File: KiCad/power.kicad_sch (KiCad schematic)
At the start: 13 parts, among them J4 10-pin power header, U1 TL074

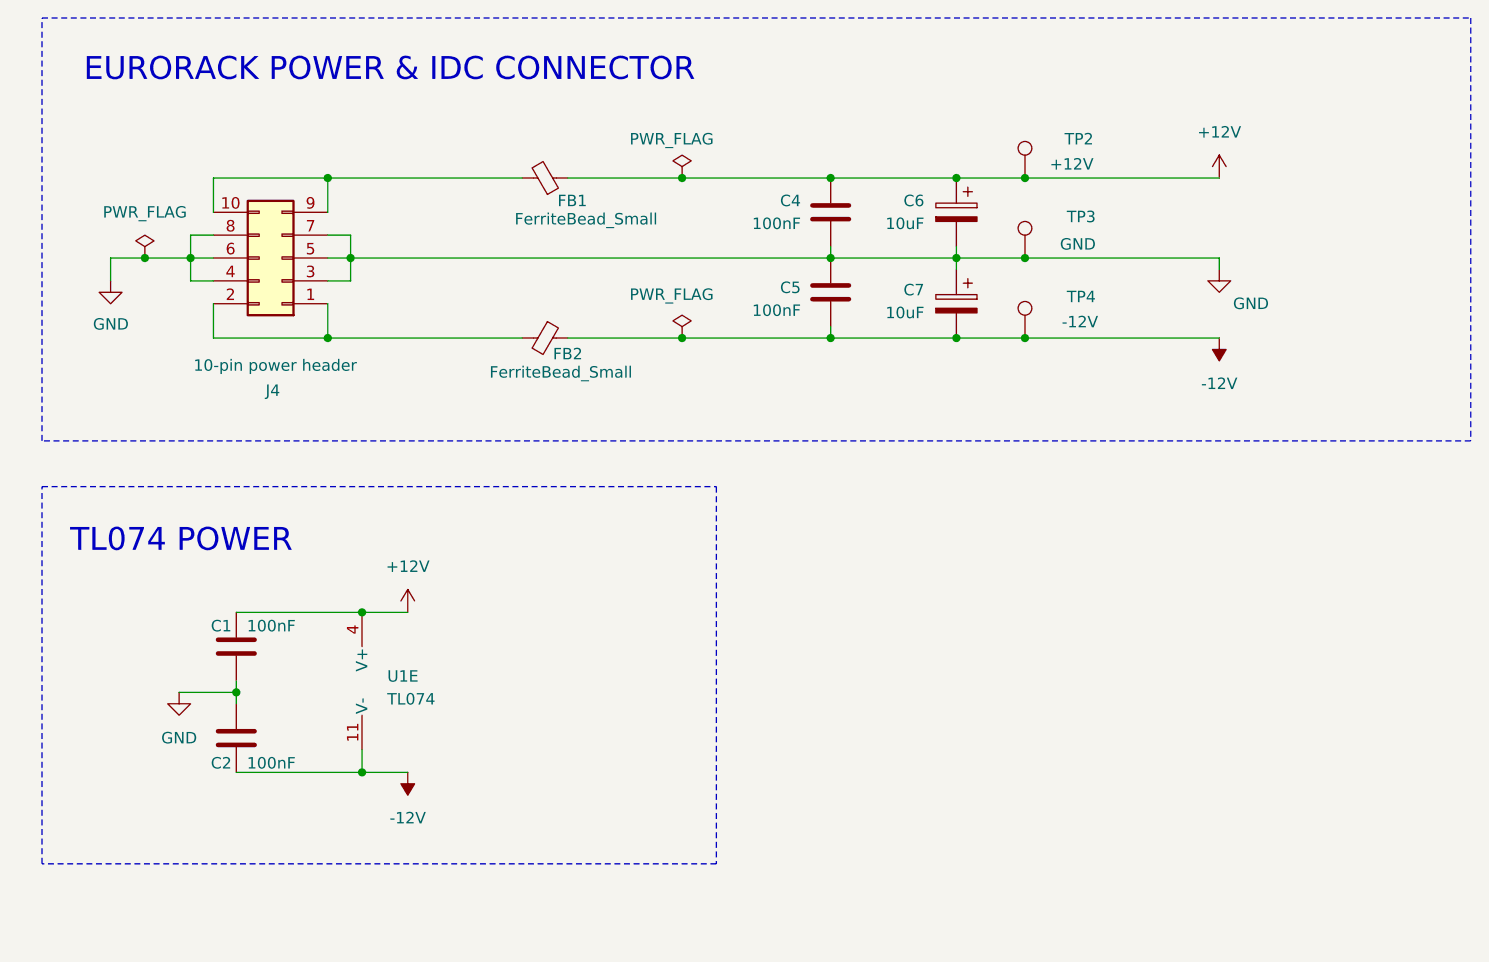
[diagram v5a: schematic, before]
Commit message: adding Test Point D
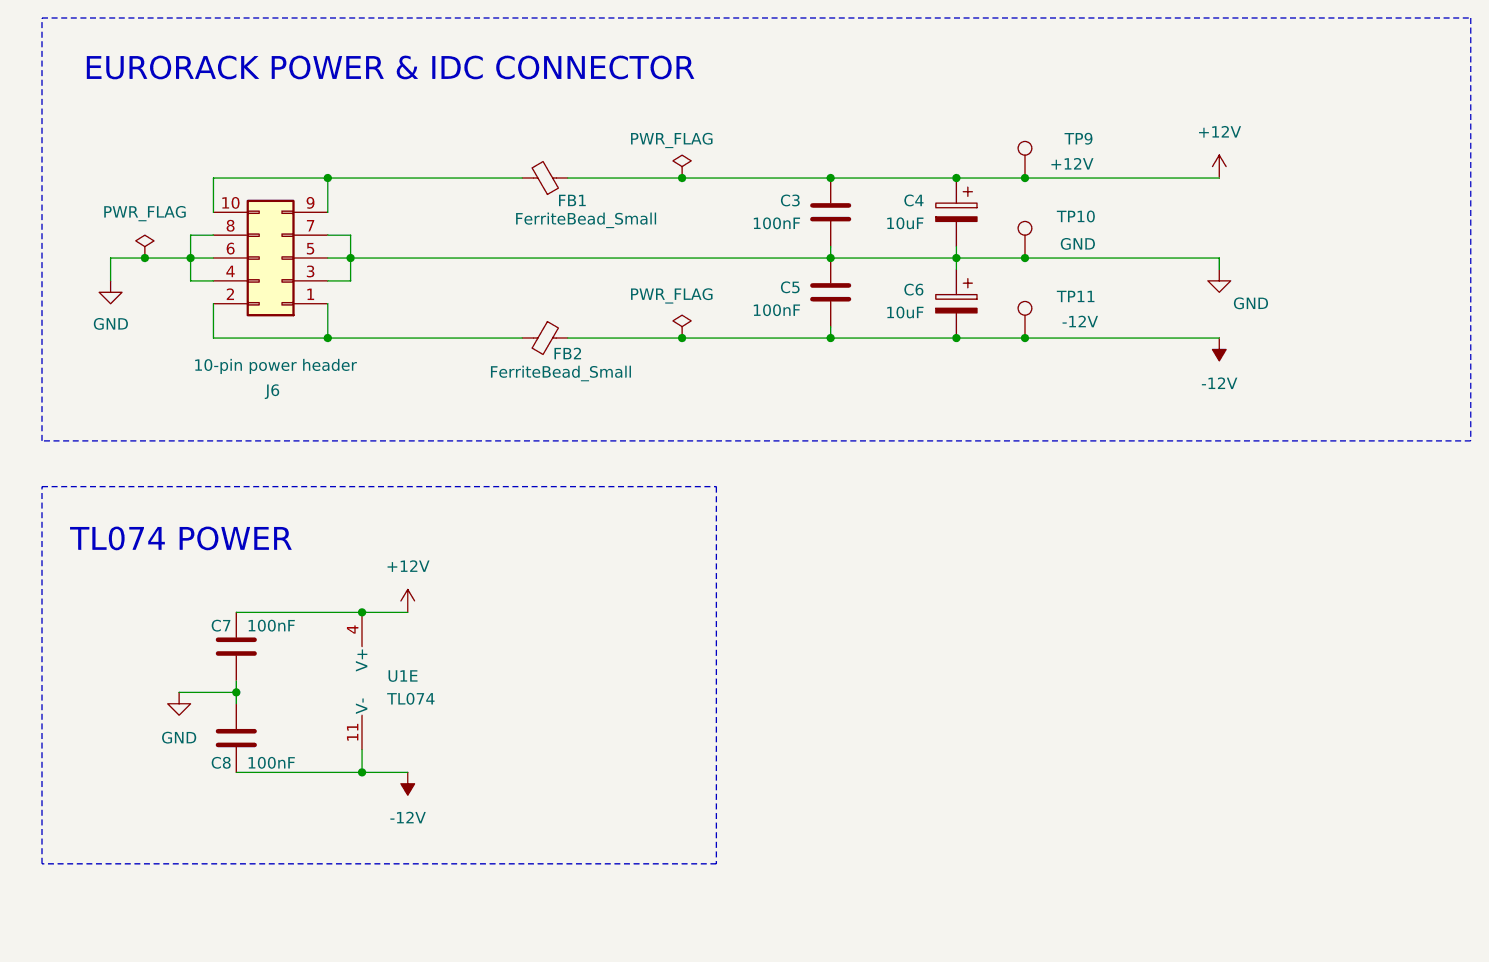
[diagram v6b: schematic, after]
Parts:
- renumbered C4 to C3, C6 to C4, C7 to C6, C1 to C7, C2 to C8, J4 to J6, TP3 to TP10, TP4 to TP11, TP2 to TP9
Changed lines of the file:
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@@
 		(on_board yes)
 		(dnp no)
-		(property "Reference" "#PWR0103"
+		(property "Reference" "#PWR020"
 			(at 147.32 55.88 0)
 			(effects
@@
 			(project ""
 				(path "/c997e785-a132-463f-bd08-a5a67a697207/6da73ad2-1669-4740-9ebd-dad26a4437f2"
-					(reference "#PWR0103")
+					(reference "#PWR020")
 					(unit 1)
 				)
@@
 		(dnp no)
 		(fields_autoplaced yes)
-		(property "Reference" "#PWR0101"
+		(property "Reference" "#PWR019"
 			(at 147.32 43.18 0)
 			(effects
@@
 			(project ""
 				(path "/c997e785-a132-463f-bd08-a5a67a697207/6da73ad2-1669-4740-9ebd-dad26a4437f2"
-					(reference "#PWR0101")
+					(reference "#PWR019")
 					(unit 1)
 				)
@@
 		(on_board yes)
 		(dnp no)
-		(property "Reference" "C4"
+		(property "Reference" "C3"
 			(at 100.838 41.91 0)
 			(effects
@@
 			(project ""
 				(path "/c997e785-a132-463f-bd08-a5a67a697207/6da73ad2-1669-4740-9ebd-dad26a4437f2"
-					(reference "C4")
+					(reference "C3")
 					(unit 1)
 				)
@@
 		(dnp no)
 		(fields_autoplaced yes)
-		(property "Reference" "#PWR0102"
+		(property "Reference" "#PWR022"
 			(at 147.32 53.34 0)
 			(effects
@@
 			(project ""
 				(path "/c997e785-a132-463f-bd08-a5a67a697207/6da73ad2-1669-4740-9ebd-dad26a4437f2"
-					(reference "#PWR0102")
+					(reference "#PWR022")
 					(unit 1)
 				)
@@
 		(dnp no)
 		(fields_autoplaced yes)
-		(property "Reference" "#FLG0102"
+		(property "Reference" "#FLG02"
 			(at 27.94 46.355 0)
 			(effects
@@
 			(project ""
 				(path "/c997e785-a132-463f-bd08-a5a67a697207/6da73ad2-1669-4740-9ebd-dad26a4437f2"
-					(reference "#FLG0102")
+					(reference "#FLG02")
 					(unit 1)
 				)
@@
 		(on_board yes)
 		(dnp no)
-		(property "Reference" "#PWR0104"
+		(property "Reference" "#PWR021"
 			(at 24.13 57.15 0)
 			(effects
@@
 			(project ""
 				(path "/c997e785-a132-463f-bd08-a5a67a697207/6da73ad2-1669-4740-9ebd-dad26a4437f2"
-					(reference "#PWR0104")
+					(reference "#PWR021")
 					(unit 1)
 				)
@@
 		(dnp no)
 		(fields_autoplaced yes)
-		(property "Reference" "#PWR030"
+		(property "Reference" "#PWR025"
 			(at 57.15 101.6 0)
 			(effects
@@
 			(project ""
 				(path "/c997e785-a132-463f-bd08-a5a67a697207/6da73ad2-1669-4740-9ebd-dad26a4437f2"
-					(reference "#PWR030")
+					(reference "#PWR025")
 					(unit 1)
 				)
@@
 		(on_board yes)
 		(dnp no)
-		(property "Reference" "C2"
+		(property "Reference" "C8"
 			(at 37.592 104.394 0)
 			(effects
@@
 			(project "sequencer"
 				(path "/c997e785-a132-463f-bd08-a5a67a697207/6da73ad2-1669-4740-9ebd-dad26a4437f2"
-					(reference "C2")
+					(reference "C8")
 					(unit 1)
 				)
@@
 		(on_board yes)
 		(dnp no)
-		(property "Reference" "C7"
+		(property "Reference" "C6"
 			(at 114.554 51.816 0)
 			(effects
@@
 			(project ""
 				(path "/c997e785-a132-463f-bd08-a5a67a697207/6da73ad2-1669-4740-9ebd-dad26a4437f2"
-					(reference "C7")
+					(reference "C6")
 					(unit 1)
 				)
@@
 		(on_board yes)
 		(dnp no)
-		(property "Reference" "TP2"
+		(property "Reference" "TP9"
 			(at 133.35 35.052 0)
 			(effects
@@
 			(project ""
 				(path "/c997e785-a132-463f-bd08-a5a67a697207/6da73ad2-1669-4740-9ebd-dad26a4437f2"
-					(reference "TP2")
+					(reference "TP9")
 					(unit 1)
 				)
@@
 		(on_board yes)
 		(dnp no)
-		(property "Reference" "TP4"
+		(property "Reference" "TP11"
 			(at 133.604 52.578 0)
 			(effects
@@
 			(project ""
 				(path "/c997e785-a132-463f-bd08-a5a67a697207/6da73ad2-1669-4740-9ebd-dad26a4437f2"
-					(reference "TP4")
+					(reference "TP11")
 					(unit 1)
 				)
@@
 		(on_board yes)
 		(dnp no)
-		(property "Reference" "#FLG0103"
+		(property "Reference" "#FLG03"
 			(at 87.63 55.245 0)
 			(effects
@@
 			(project ""
 				(path "/c997e785-a132-463f-bd08-a5a67a697207/6da73ad2-1669-4740-9ebd-dad26a4437f2"
-					(reference "#FLG0103")
+					(reference "#FLG03")
 					(unit 1)
 				)
@@
 		(on_board yes)
 		(dnp no)
-		(property "Reference" "C1"
+		(property "Reference" "C7"
 			(at 37.592 89.154 0)
 			(effects
@@
 			(project "sequencer"
 				(path "/c997e785-a132-463f-bd08-a5a67a697207/6da73ad2-1669-4740-9ebd-dad26a4437f2"
-					(reference "C1")
+					(reference "C7")
 					(unit 1)
 				)
@@
 		(dnp no)
 		(fields_autoplaced yes)
-		(property "Reference" "#PWR011"
+		(property "Reference" "#PWR023"
 			(at 57.15 91.44 0)
 			(effects
@@
 			(project "sequencer"
 				(path "/c997e785-a132-463f-bd08-a5a67a697207/6da73ad2-1669-4740-9ebd-dad26a4437f2"
-					(reference "#PWR011")
+					(reference "#PWR023")
 					(unit 1)
 				)
@@
 		(dnp no)
 		(fields_autoplaced yes)
-		(property "Reference" "#PWR04"
+		(property "Reference" "#PWR024"
 			(at 31.75 102.87 0)
 			(effects
@@
 			(project "sequencer"
 				(path "/c997e785-a132-463f-bd08-a5a67a697207/6da73ad2-1669-4740-9ebd-dad26a4437f2"
-					(reference "#PWR04")
+					(reference "#PWR024")
 					(unit 1)
 				)
@@
 		(on_board yes)
 		(dnp no)
-		(property "Reference" "#FLG0101"
+		(property "Reference" "#FLG01"
 			(at 87.63 37.465 0)
 			(effects
@@
 			(project ""
 				(path "/c997e785-a132-463f-bd08-a5a67a697207/6da73ad2-1669-4740-9ebd-dad26a4437f2"
-					(reference "#FLG0101")
+					(reference "#FLG01")
 					(unit 1)
 				)
@@
 		(on_board yes)
 		(dnp no)
-		(property "Reference" "J4"
+		(property "Reference" "J6"
 			(at 42.164 62.992 0)
 			(effects
@@
 			(project ""
 				(path "/c997e785-a132-463f-bd08-a5a67a697207/6da73ad2-1669-4740-9ebd-dad26a4437f2"
-					(reference "J4")
+					(reference "J6")
 					(unit 1)
 				)
@@
 		(on_board yes)
 		(dnp no)
-		(property "Reference" "C6"
+		(property "Reference" "C4"
 			(at 114.554 41.91 0)
 			(effects
@@
 			(project ""
 				(path "/c997e785-a132-463f-bd08-a5a67a697207/6da73ad2-1669-4740-9ebd-dad26a4437f2"
-					(reference "C6")
+					(reference "C4")
 					(unit 1)
 				)
@@
 		(on_board yes)
 		(dnp no)
-		(property "Reference" "TP3"
+		(property "Reference" "TP10"
 			(at 133.604 43.688 0)
 			(effects
@@
 			(project ""
 				(path "/c997e785-a132-463f-bd08-a5a67a697207/6da73ad2-1669-4740-9ebd-dad26a4437f2"
-					(reference "TP3")
+					(reference "TP10")
 					(unit 1)
 				)
